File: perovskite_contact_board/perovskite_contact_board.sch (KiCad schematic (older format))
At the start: 14 parts, among them J1 Conn_01x08, J2 Conn_01x08, J3 Conn_01x08, J4 Conn_01x08, J5 Conn_01x08, J6 Conn_01x08, U1 Perovskite_CP_6_Cell, U2 Perovskite_CP_6_Cell, U3 Perovskite_CP_6_Cell, U4 MCP9808_MSOP, U5 MCP9808_MSOP, U6 MCP9808_MSOP

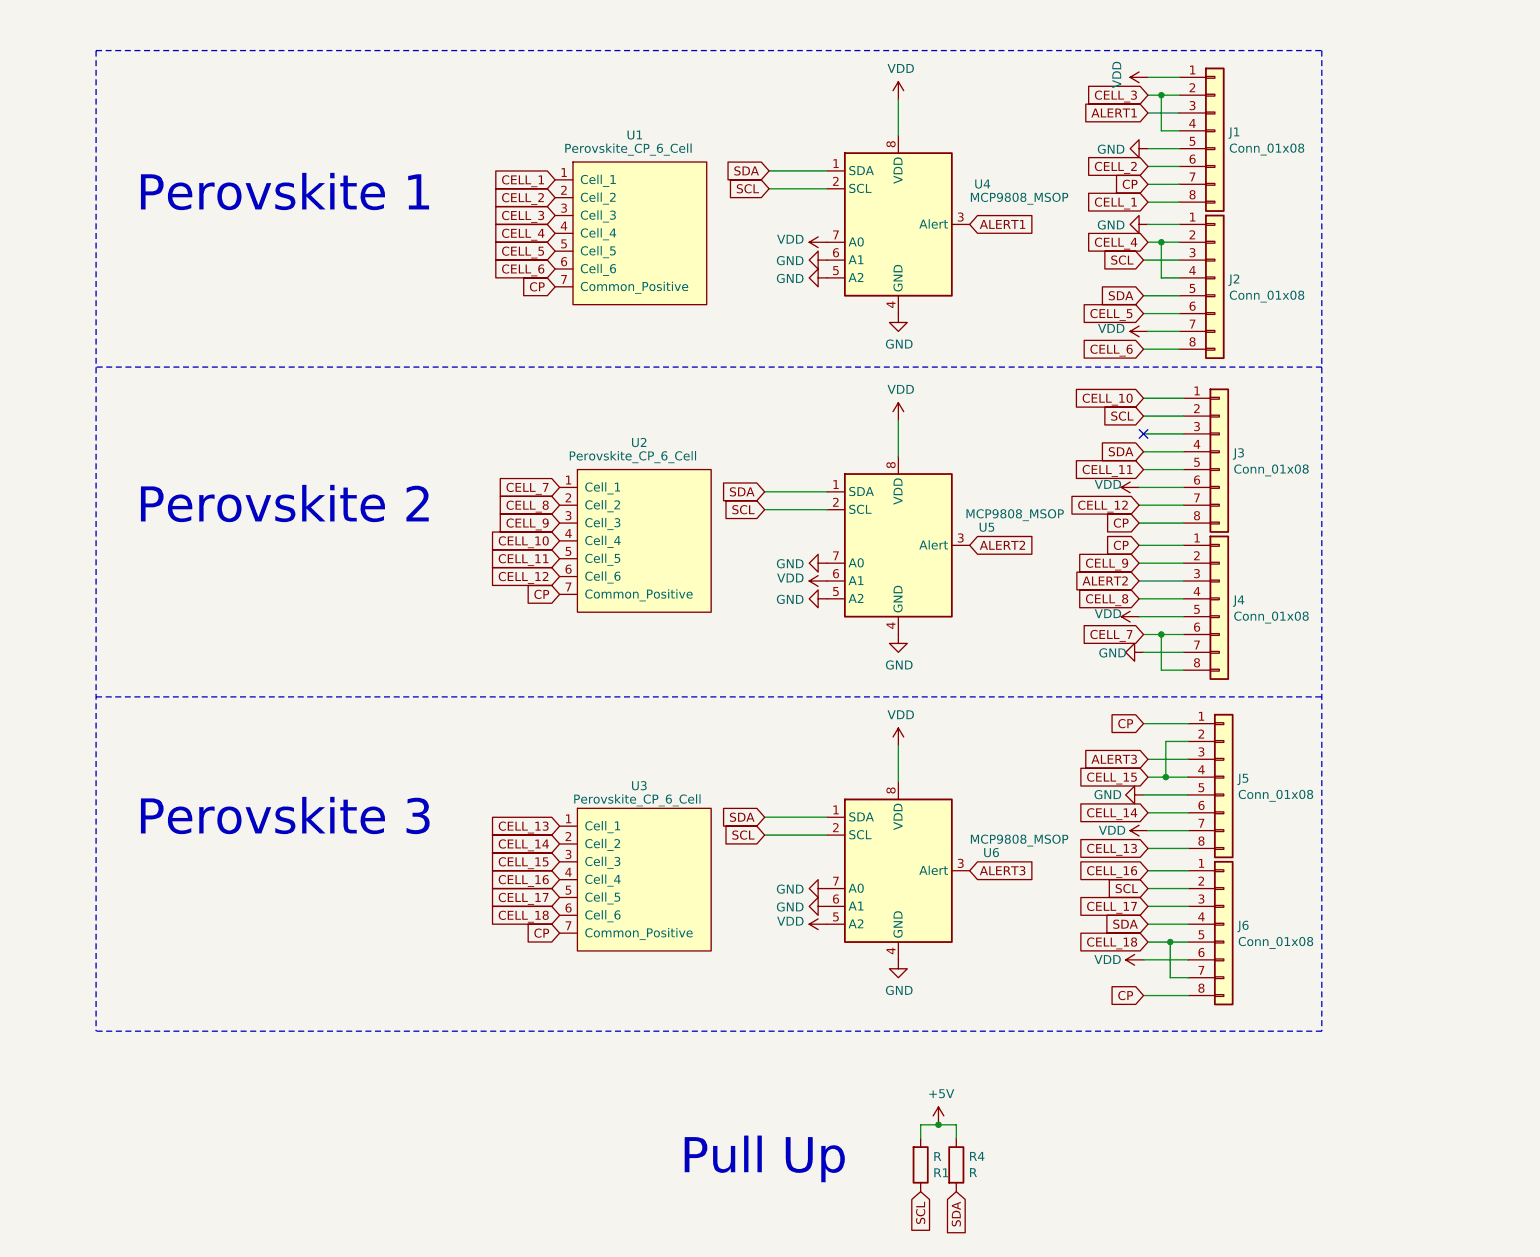
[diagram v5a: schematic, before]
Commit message: contact board oriented correctly
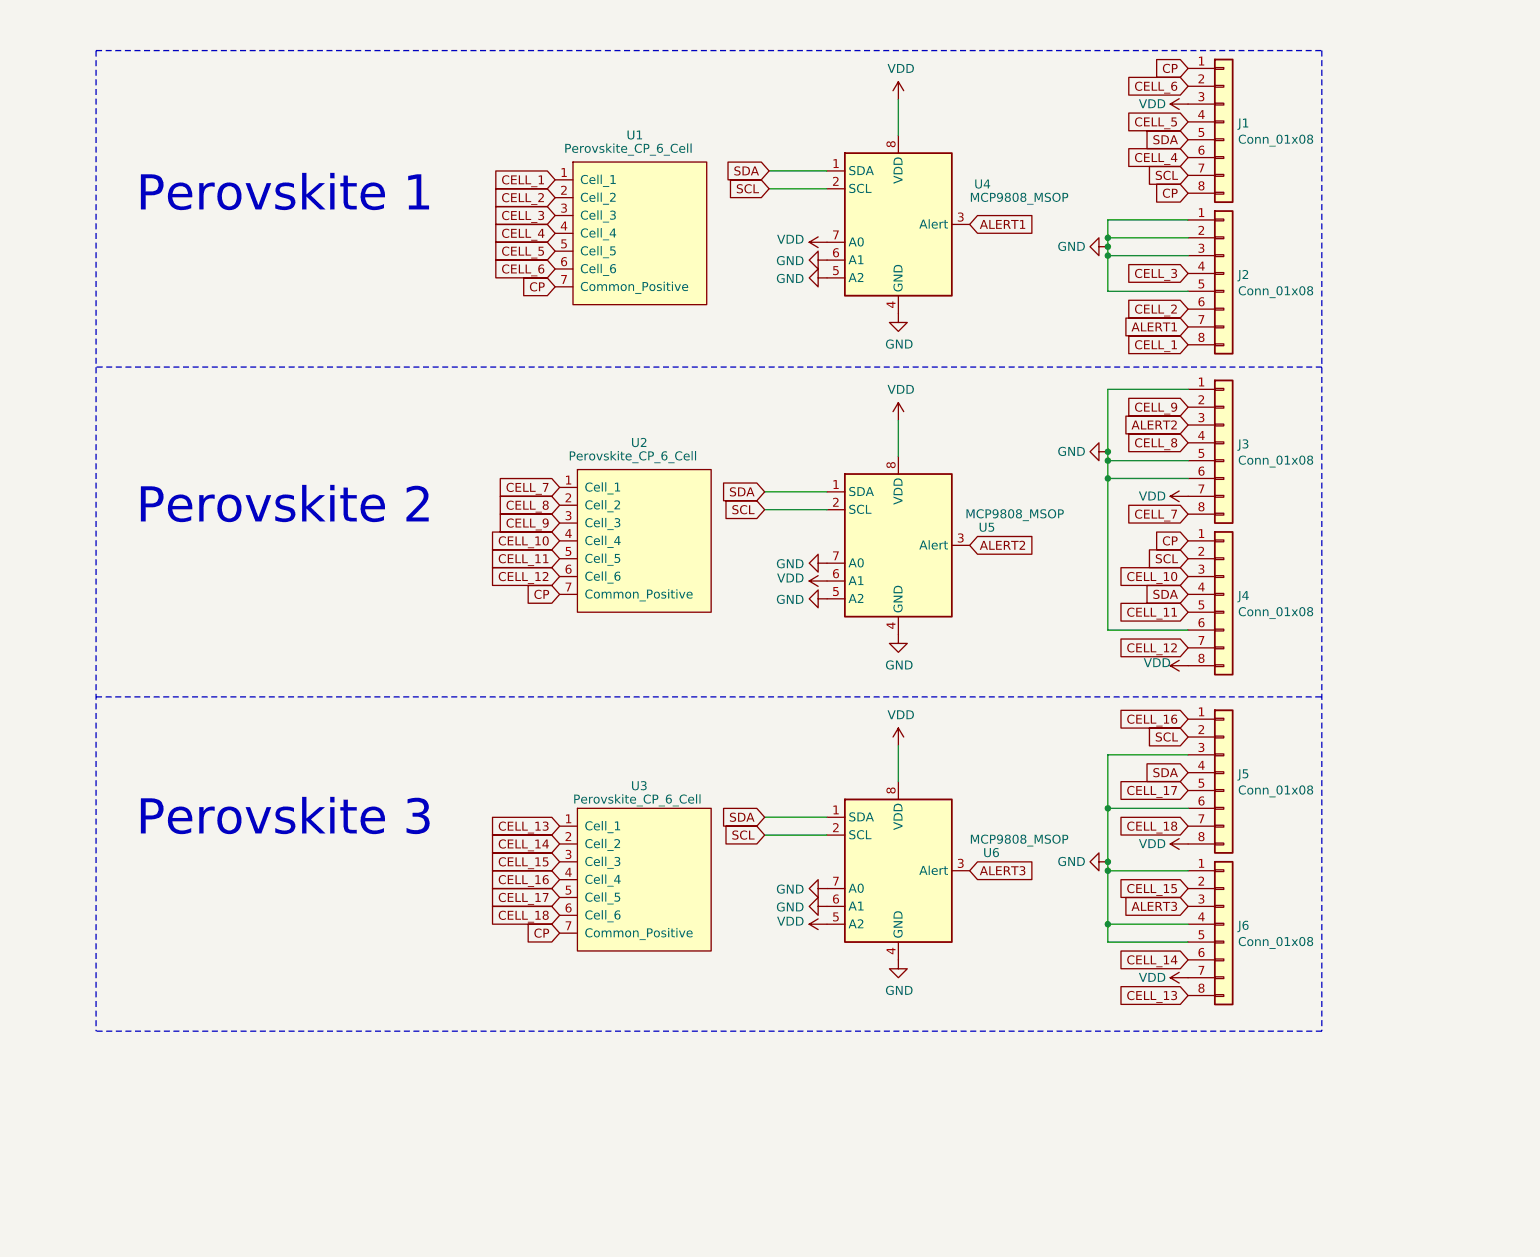
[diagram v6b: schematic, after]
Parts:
- removed R1, R4: R, Resistor_SMD:R_0603_1608Metric, symbol Device:R
- J2: footprint Connector_PinSocket_2.54mm:PinSocket_1x08_P2.54mm_Vertical_SMD_Pin1Right -> Connector_PinHeader_2.54mm:PinHeader_1x08_P2.54mm_Vertical_SMD_Pin1Left
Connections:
- net ALERT1: now also J2.7 (Pin_7); no longer J1.3 (Pin_3)
- net ALERT2: now also J3.3 (Pin_3); no longer J4.3 (Pin_3)
- net ALERT3: now also J6.3 (Pin_3); no longer J5.3 (Pin_3)
- net CELL_1: now also J2.8 (Pin_8); no longer J1.8 (Pin_8)
- net CELL_10: now also J4.3 (Pin_3); no longer J3.1 (Pin_1)
- net CELL_11: now also J4.5 (Pin_5); no longer J3.5 (Pin_5)
- net CELL_12: now also J4.7 (Pin_7); no longer J3.7 (Pin_7)
- net CELL_13: now also J6.8 (Pin_8); no longer J5.8 (Pin_8)
- net CELL_14: now also J6.6 (Pin_6); no longer J5.6 (Pin_6)
- net CELL_15: now also J6.2 (Pin_2); no longer J5.2 (Pin_2), J5.4 (Pin_4)
- net CELL_16: now also J5.1 (Pin_1); no longer J6.1 (Pin_1)
- net CELL_17: now also J5.5 (Pin_5); no longer J6.3 (Pin_3)
- net CELL_18: now also J5.7 (Pin_7); no longer J6.5 (Pin_5), J6.7 (Pin_7)
- net CELL_2: now also J2.6 (Pin_6); no longer J1.6 (Pin_6)
- net CELL_3: now also J2.4 (Pin_4); no longer J1.2 (Pin_2), J1.4 (Pin_4)
- net CELL_4: now also J1.6 (Pin_6); no longer J2.2 (Pin_2), J2.4 (Pin_4)
- net CELL_5: now also J1.4 (Pin_4); no longer J2.6 (Pin_6)
- net CELL_6: now also J1.2 (Pin_2); no longer J2.8 (Pin_8)
- net CELL_7: now also J3.8 (Pin_8); no longer J4.6 (Pin_6), J4.8 (Pin_8)
- net CELL_8: now also J3.4 (Pin_4); no longer J4.4 (Pin_4)
- net CELL_9: now also J3.2 (Pin_2); no longer J4.2 (Pin_2)
- net CP: now also J1.1 (Pin_1), J1.8 (Pin_8); no longer J1.7 (Pin_7), J3.8 (Pin_8), J5.1 (Pin_1), J6.8 (Pin_8)
- net GND: now also J2.2 (Pin_2), J2.3 (Pin_3), J2.5 (Pin_5), J3.1 (Pin_1), J3.5 (Pin_5), J3.6 (Pin_6), J4.6 (Pin_6), J5.3 (Pin_3), J5.6 (Pin_6), J6.1 (Pin_1), J6.4 (Pin_4), J6.5 (Pin_5); no longer J1.5 (Pin_5), J4.7 (Pin_7), J5.5 (Pin_5)
- net SCL: now also J1.7 (Pin_7), J4.2 (Pin_2), J5.2 (Pin_2); no longer J2.3 (Pin_3), J3.2 (Pin_2), J6.2 (Pin_2)
- net SDA: now also J1.5 (Pin_5), J4.4 (Pin_4), J5.4 (Pin_4); no longer J2.5 (Pin_5), J3.4 (Pin_4), J6.4 (Pin_4)
- net VDD: now also J1.3 (Pin_3), J3.7 (Pin_7), J4.8 (Pin_8), J5.8 (Pin_8), J6.7 (Pin_7); no longer J1.1 (Pin_1), J2.7 (Pin_7), J3.6 (Pin_6), J4.5 (Pin_5), J5.7 (Pin_7), J6.6 (Pin_6)
- no-connect marks 1 -> 0
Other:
- note removed: "Pull Up"
- moved on the sheet: J1, J2, J3, J4, J5

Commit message: Updating designs
- Generate gerbers
- Generate renders
- Working on layout for payload controller
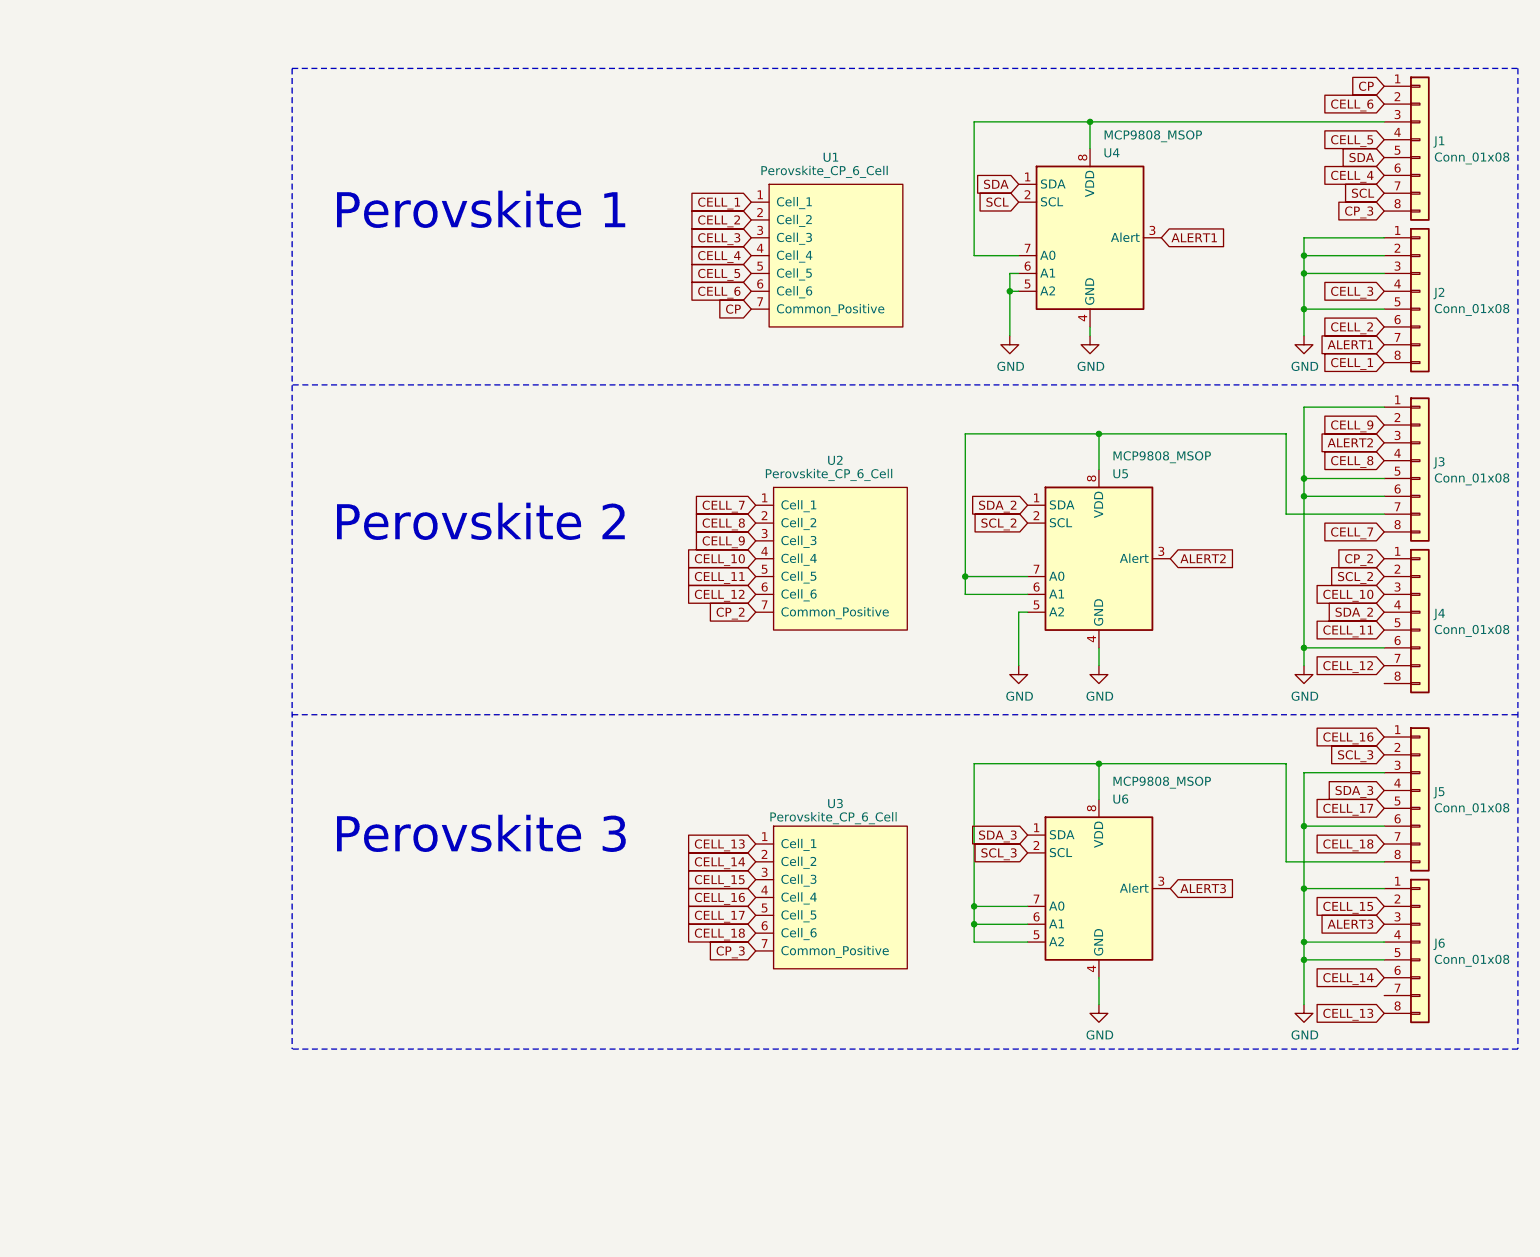
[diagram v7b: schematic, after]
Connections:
- net CP: no longer J1.8 (Pin_8), J4.1 (Pin_1), U2.7 (Common_Positive), U3.7 (Common_Positive)
- net GND: no longer U5.7 (A0), U6.6 (A1), U6.7 (A0)
- net SCL: no longer J4.2 (Pin_2), J5.2 (Pin_2), U5.2 (SCL), U6.2 (SCL)
- net SDA: no longer J4.4 (Pin_4), J5.4 (Pin_4), U5.1 (SDA), U6.1 (SDA)
- removed net VDD: J1.3 (Pin_3), J3.7 (Pin_7), J4.8 (Pin_8), J5.8 (Pin_8), J6.7 (Pin_7), U4.7 (A0), U4.8 (VDD), U5.6 (A1), U5.8 (VDD), U6.5 (A2), U6.8 (VDD)
- new net: J1.3 (Pin_3), U4.7 (A0), U4.8 (VDD)
- new net: J3.7 (Pin_7), U5.6 (A1), U5.7 (A0), U5.8 (VDD)
- new net: J5.8 (Pin_8), U6.5 (A2), U6.6 (A1), U6.7 (A0), U6.8 (VDD)
- new net CP_2: J4.1 (Pin_1), U2.7 (Common_Positive)
- new net CP_3: J1.8 (Pin_8), U3.7 (Common_Positive)
- new net SCL_2: J4.2 (Pin_2), U5.2 (SCL)
- new net SCL_3: J5.2 (Pin_2), U6.2 (SCL)
- new net SDA_2: J4.4 (Pin_4), U5.1 (SDA)
- new net SDA_3: J5.4 (Pin_4), U6.1 (SDA)
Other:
- moved on the sheet: J1, J2, J3, J4, J5, J6, U1, U2, U3, U4, U5, U6
